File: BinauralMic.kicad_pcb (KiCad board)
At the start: 4 copper layers, 63.8 x 62.8 mm, 59 parts, among them IC1 PCM2903CDBR, J1 RCJ-017, J2 USB4105-GF-A-120, J3 Conn_01x02_Pin, J4 Conn_01x02_Pin, U1 MIC5504-3.3YM5, U2 TL972QDRQ1, U3 74LVC1G08, X1 ECS-120-8-36-CKM-TR3

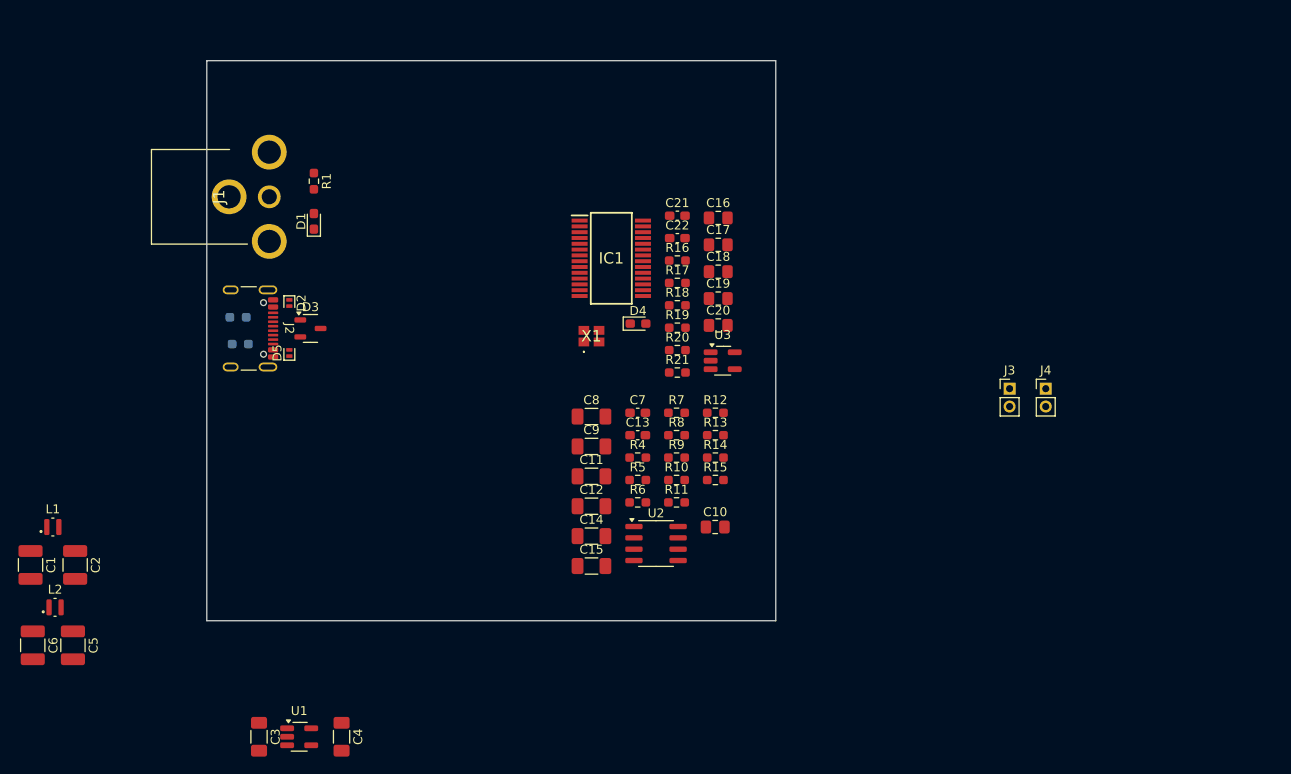
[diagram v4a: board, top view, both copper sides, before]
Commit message: Removed S/PIDF and still doing layout
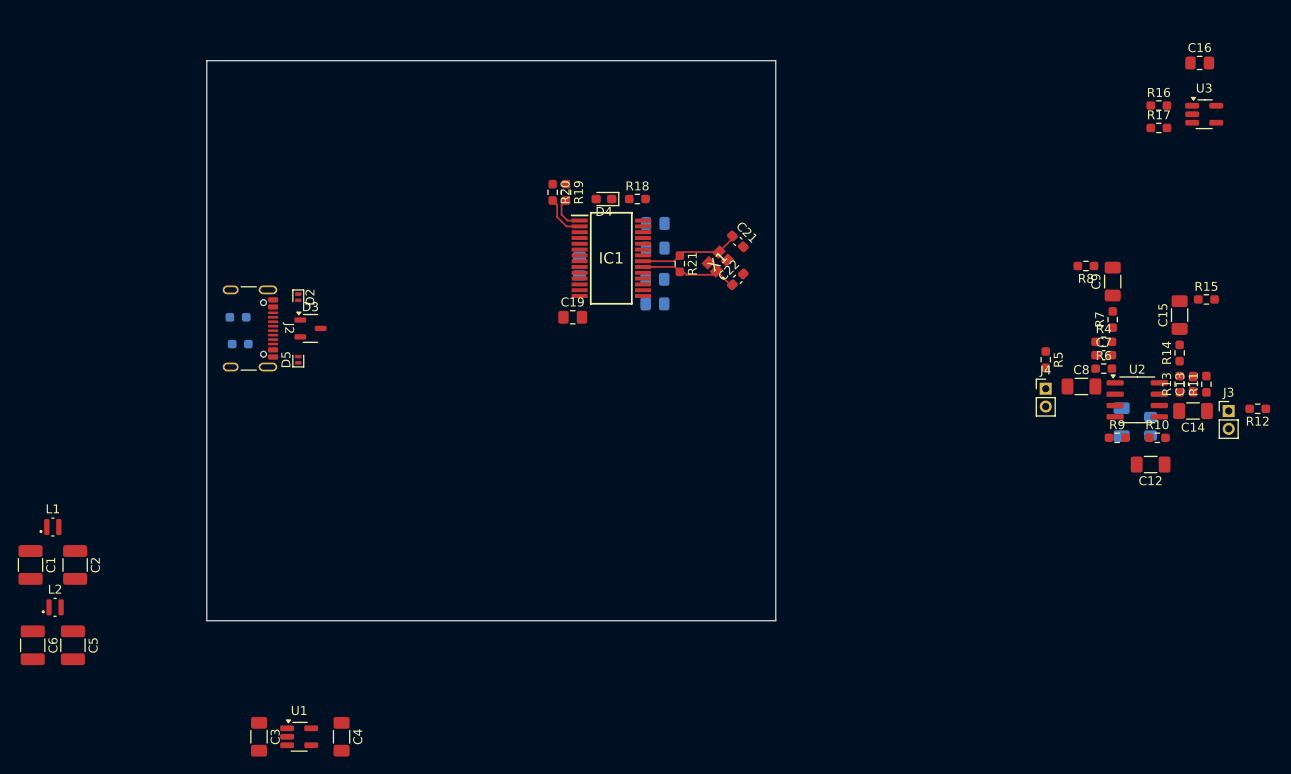
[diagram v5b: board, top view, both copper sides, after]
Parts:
- removed D1: CG0603MLU-3.3E, Diode_SMD:D_0603_1608Metric_Pad1.05x0.95mm_HandSolder
- removed J1: RCJ-017, binauralmic:RCJ014
- removed R1: 75, Resistor_SMD:R_0603_1608Metric_Pad0.98x0.95mm_HandSolder
- added C23: 10u, Capacitor_SMD:C_0805_2012Metric_Pad1.18x1.45mm_HandSolder, B.Cu at (151.0, 80.2)
- added C24: 10u, Capacitor_SMD:C_0805_2012Metric_Pad1.18x1.45mm_HandSolder, B.Cu at (151.0, 74.0)
- C10, C11, C17, C18, C20: moved to B.Cu
- moved C15 71.6 mm to (209.8, 81.5), turned to 90 degrees
- moved C14 68.8 mm to (211.2, 92.2), turned to 180 degrees
- moved C12 62.8 mm to (206.5, 98.2), turned to 180 degrees
- moved C13 62.5 mm to (211.2, 89.2), turned to 90 degrees
- moved C9 61.2 mm to (202.2, 77.8), turned to 90 degrees
- moved R11 60.8 mm to (212.8, 89.2), turned to 90 degrees
- moved R12 60.8 mm to (218.5, 92.0), turned to 180 degrees
- moved U3 60.6 mm to (212.5, 59.0)
- moved C11 59.7 mm to (203.2, 93.5), turned to -90 degrees
- moved R15 58.6 mm to (212.8, 79.8)
- moved C16 56.7 mm to (212.0, 53.3)
- moved R16 56.7 mm to (207.4, 58.0)
- moved R17 56.7 mm to (207.4, 60.5)
- moved U2 56.3 mm to (205.0, 91.0)
- moved C8 55.0 mm to (198.8, 89.5)
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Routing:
- net /USB ADC/XTI: track 0.00 -> 11.4 mm
- net /USB ADC/XTO: track 0.00 -> 11.2 mm
- net /USB ADC/D-_R: track 0.00 -> 5.01 mm
- net /USB ADC/D+_R: track 0.00 -> 4.09 mm

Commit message: More layout, replaced chip crystal with a 2-pin oscillator
All is well with the world
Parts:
- removed X1: ECS-120-8-36-CKM-TR3, binauralmic:ECS120836CKMTR3
- added Y1: ABLS-12.000MHZ-20-D-3-H-T, binauralmic:ABLS, F.Cu at (133.5, 62.0)
- C10, C11, C17, C18, C20, C23, C24: moved to F.Cu
- moved C2 44.4 mm to (106.8, 70.2), turned to 180 degrees
- moved C1 42.9 mm to (106.8, 75.2), turned to 180 degrees
- moved L1 42.6 mm to (111.0, 72.8), turned to 90 degrees
- moved C21 31.6 mm to (129.2, 67.0), turned to 180 degrees
- moved C22 24.8 mm to (137.8, 67.0), turned to 0 degrees
- moved R18 24.8 mm to (124.9, 74.1)
- moved C17 22.3 mm to (128.8, 70.3), turned to 90 degrees
- moved R21 22.1 mm to (133.5, 67.0), turned to 0 degrees
- moved R20 21.6 mm to (125.6, 84.2), turned to 0 degrees
- moved R19 21.1 mm to (125.6, 82.2), turned to 0 degrees
- moved D4 20.6 mm to (124.9, 71.3), turned to 0 degrees
- moved C24 19.8 mm to (131.5, 70.3), turned to 90 degrees
- moved C18 17.3 mm to (135.2, 70.3), turned to 90 degrees
- moved C23 16.5 mm to (137.8, 70.3), turned to 90 degrees
- moved IC1 13.3 mm to (133.0, 77.5), turned to 90 degrees
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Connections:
- C10 pad 1: VCC -> +3.3VA
- C11 pad 1: VCC -> +3.3VA
- C16 pad 2: VDD -> VCC
- C17 pad 1: VDD -> VCC
- C6 pad 1: VDD -> +3.3VA
- D4 pad 2: VDD -> VCC
- IC1 pad 27: VDD -> VCC
- IC1 pad 3: VDD -> VCC
- IC1 pad 8: VDD -> VCC
- L2 pad 1: VDD -> +3.3VA
- R9 pad 1: VCC -> +3.3VA
- U2 pad 8: VCC -> +3.3VA
- U3 pad 1: VDD -> VCC
- U3 pad 5: VDD -> VCC
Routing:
- net GND: track 0.00 -> 21.1 mm
- net VCC: track 0.00 -> 14.9 mm
- net /USB ADC/XTO: track 11.2 -> 15.7 mm
- net /USB ADC/XTI: track 11.4 -> 15.3 mm

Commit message: Layout changes
See previous commit
I forgot to save lol
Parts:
- moved C17 9.00 mm to (119.8, 70.1)
- moved C18 9.00 mm to (126.2, 70.1)
- moved C19 9.00 mm to (134.5, 82.5)
- moved C20 9.00 mm to (125.5, 84.5)
- moved C21 9.00 mm to (120.2, 66.8)
- moved C22 9.00 mm to (128.8, 66.8)
- moved C23 9.00 mm to (128.8, 70.1)
- moved C24 9.00 mm to (122.5, 70.1)
- moved D4 9.00 mm to (115.9, 71.1)
- moved IC1 9.00 mm to (124.0, 77.2)
- moved R18 9.00 mm to (115.9, 73.8)
- moved R19 9.00 mm to (116.6, 82.0)
- moved R20 9.00 mm to (116.6, 84.0)
- moved R21 9.00 mm to (124.5, 66.8)
- moved Y1 9.00 mm to (124.5, 61.8)

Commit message: Did a lot of layout
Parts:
- moved R12 101.2 mm to (118.1, 104.3), turned to 90 degrees
- moved J3 97.8 mm to (117.8, 101.1), turned to -90 degrees
- moved C12 94.9 mm to (111.8, 92.3), turned to 90 degrees
- moved C14 93.6 mm to (117.8, 97.1), turned to 90 degrees
- moved R10 92.5 mm to (114.8, 93.1), turned to -90 degrees
- moved R11 92.4 mm to (120.8, 98.6), turned to 0 degrees
- moved C13 90.8 mm to (120.8, 97.1), turned to 0 degrees
- moved R13 89.2 mm to (120.8, 95.6), turned to 0 degrees
- moved R9 88.2 mm to (114.8, 88.6), turned to -90 degrees
- moved C4 86.6 mm to (157.8, 53.0), turned to 0 degrees
- moved R14 86.0 mm to (124.3, 95.6), turned to 0 degrees
- moved U2 85.9 mm to (119.1, 90.8), turned to -90 degrees
- moved U1 85.0 mm to (157.8, 57.7), turned to 90 degrees
- moved R15 84.6 mm to (130.3, 98.6), turned to -90 degrees
- moved C3 84.0 mm to (157.8, 62.2), turned to 0 degrees
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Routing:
- net /VBUS: track 0.00 -> 56.7 mm, vias 0 -> 5
- net GND: track 21.1 -> 39.4 mm, vias 0 -> 9
- net /D+: track 0.00 -> 14.3 mm
- net VCC: track 14.9 -> 27.0 mm, vias 0 -> 9
- net /D-: track 0.00 -> 11.5 mm, vias 0 -> 2
- net /USB ADC/~{SSPND}: track 0.00 -> 5.97 mm
- net +5V: track 0.00 -> 3.69 mm
- net /USB ADC/D+_PUR: track 0.00 -> 3.48 mm
- net /Connectors/CC1: track 0.00 -> 2.96 mm, vias 0 -> 1
- net /Connectors/CC2: track 0.00 -> 2.77 mm, vias 0 -> 1
- net /USB ADC/~{SSPND}_R: track 0.00 -> 2.22 mm
- added copper zone on F.Cu, net +5V
- added copper zone on F.Cu, net /VBUS
- added copper zone on B.Cu, net GND
- added copper zone on F.Cu, net GND
- added copper zone on In1.Cu, net GND
- added copper zone on F.Cu, net VCC
- added copper zone on In2.Cu, net VCC
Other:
- board size 63.8 x 62.8 mm -> 58 x 63.8 mm
